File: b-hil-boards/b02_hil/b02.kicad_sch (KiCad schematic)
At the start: 13 parts, among them J2 Conn_01x06_Socket, K1 Relay_DPDT, K2 Relay_DPDT, K3 Relay_DPDT, K4 Relay_DPDT, U1 MAX485E, U2 ULN2003, U3 ADuM1412, U4 ESP32_C3_SuperMini, U5 OLED-128x64-I2C

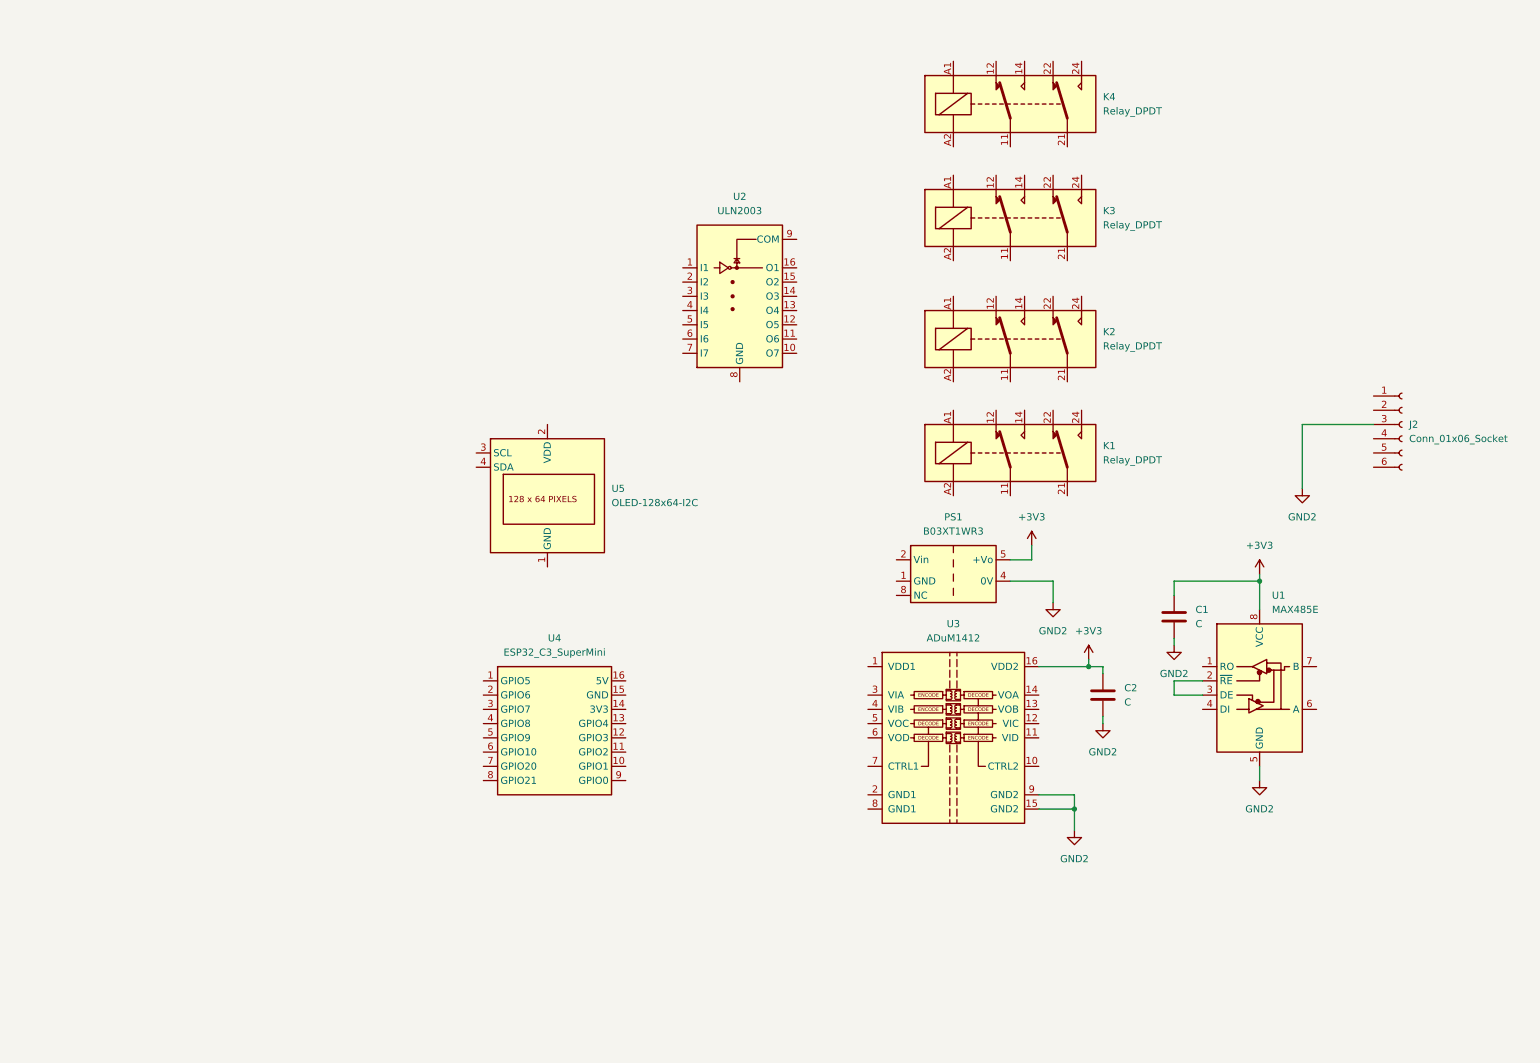
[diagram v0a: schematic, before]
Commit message: B02 card: routing and silkscreen completed
- PCB layout and silkscreen finished for b02_hil
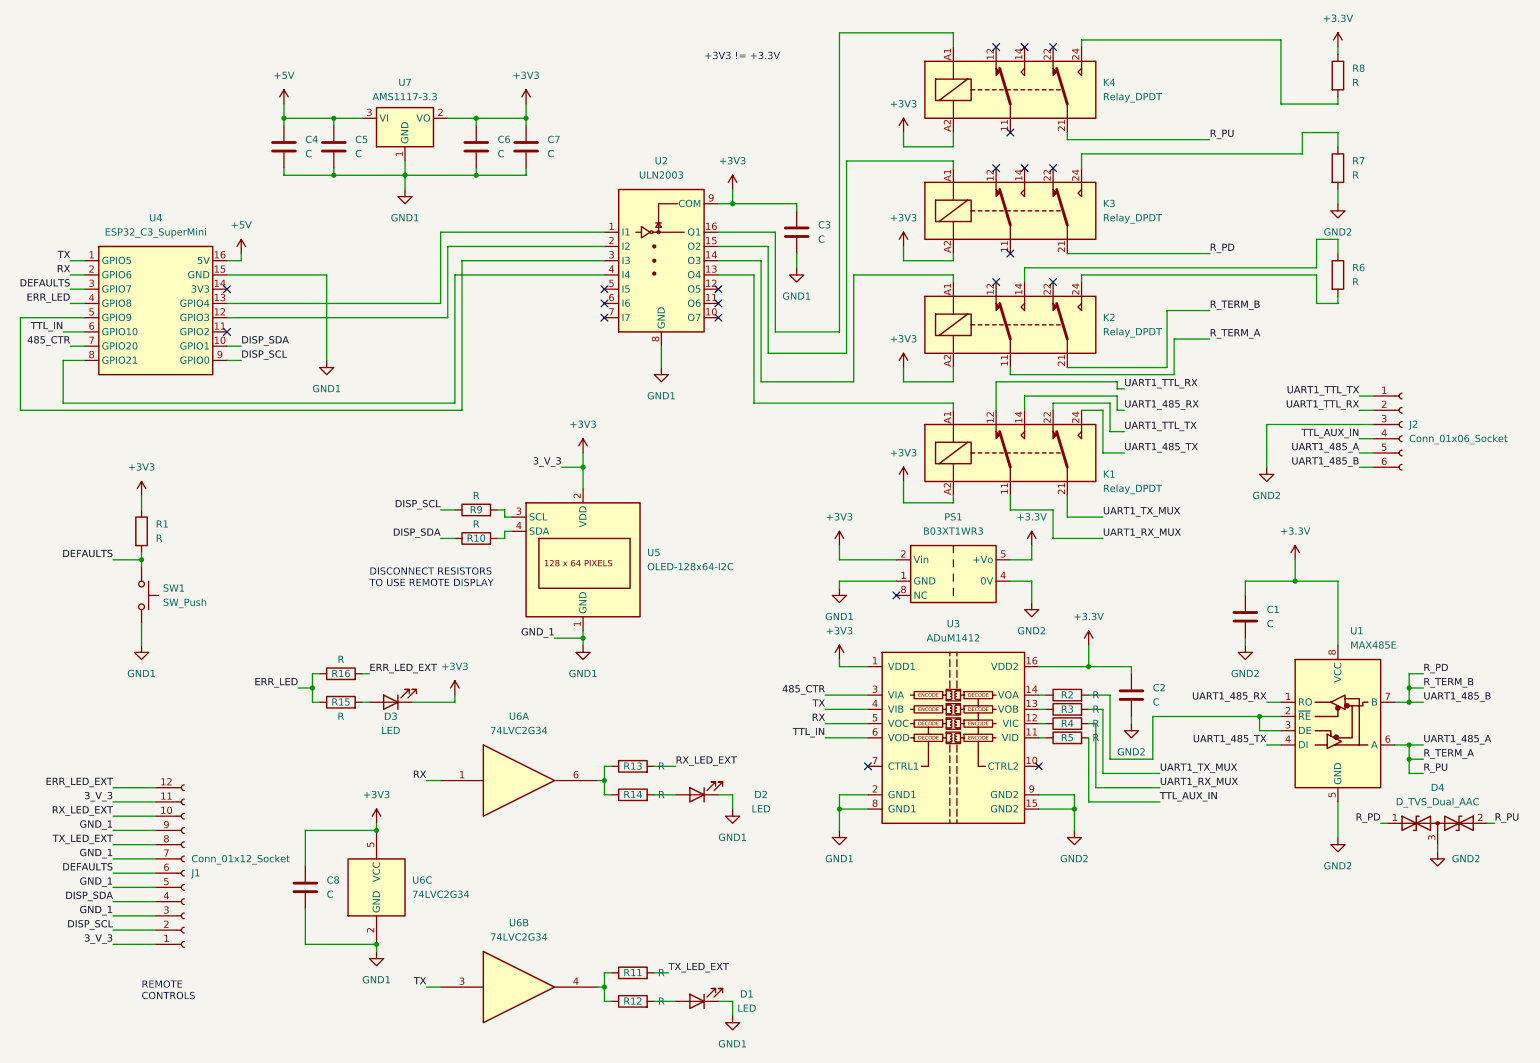
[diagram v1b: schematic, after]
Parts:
- added C3, C4, C5, C6, C7, C8: C, Capacitor_SMD:C_0805_2012Metric_Pad1.18x1.45mm_HandSolder, symbol Device:C
- added D1, D2, D3: LED, LED_SMD:LED_0805_2012Metric_Pad1.15x1.40mm_HandSolder, symbol Device:LED
- added D4: D_TVS_Dual_AAC, Package_TO_SOT_SMD:SOT-23-3, symbol Device:D_TVS_Dual_AAC
- added J1: Conn_01x12_Socket, TerminalBlock_DoubleLevel:TerminalBlock_DoubleLevel_2x06_P3.50mm_Horizontal, symbol Connector:Conn_01x12_Socket
- added R1, R10, R11, R12, R13, R14, R15, R16, R2, R3, R4, R5, R6, R7, R8, R9: R, Resistor_SMD:R_0805_2012Metric_Pad1.20x1.40mm_HandSolder, symbol Device:R
- added SW1: SW_Push, Button_Switch_SMD:SW_Push_1P1T_NO_6x6mm_H9.5mm, symbol Switch:SW_Push
- added U6: 74LVC2G34, Package_TO_SOT_SMD:SOT-23-6_Handsoldering, symbol 74xGxx:74LVC2G34
- added U7: AMS1117-3.3, Package_TO_SOT_SMD:SOT-223-3_TabPin2, symbol Regulator_Linear:AMS1117-3.3
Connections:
- net +3V3: now also K1.A2, K2.A2, K3.A2, K4.A2, PS1.2 (Vin), U2.9 (COM), U3.1 (VDD1), U5.2 (VDD), C3.1, C6.1, C7.1, C8.1, D3.1 (K), J1.1 (Pin_1), J1.11 (Pin_11), R1.1, U6.5 (VCC), U7.2 (VO); no longer C1.1, C2.1, PS1.5 (+Vo), U1.8 (VCC), U3.16 (VDD2)
- net GND2: now also D4.3 (common), R7.2
- net R_PU: now reaches K4.21
- net R_PU: now also J2.5 (Pin_5), K2.11, U1.6 (A), D4.2 (A2)
- net at K4.24: now also R8.2
- net at K4.A1: now also U2.16 (O1)
- net GND1: now reaches U5.1 (GND)
- net GND1: now also PS1.1 (GND), U2.8 (GND), U3.2 (GND1), U3.8 (GND1), U4.15 (GND), C3.2, C4.2, C5.2, C6.2, C7.2, C8.2, D1.1 (K), D2.1 (K), J1.3 (Pin_3), J1.5 (Pin_5), J1.7 (Pin_7), J1.9 (Pin_9), SW1.2, U6.2 (GND), U7.1 (GND)
- net at U5.3 (SCL): now also R9.2
- net at U5.4 (SDA): now also R10.2
- net UART1_TTL_TX: now reaches J2.1 (Pin_1)
- net UART1_TTL_TX: now also K1.22
- net UART1_TTL_RX: now reaches J2.2 (Pin_2)
- net UART1_TTL_RX: now also K1.12
- net TTL_AUX_IN: now reaches J2.4 (Pin_4)
- net TTL_AUX_IN: now also R5.2
- net R_PD: now reaches J2.6 (Pin_6)
- net R_PD: now also K2.21, K3.21, U1.7 (B), D4.1 (A1)
- net at U2.1 (I1): now also U4.13 (GPIO4)
- net at U2.13 (O4): now also K1.A1
- net at U2.14 (O3): now also K2.A1
- net at U2.15 (O2): now also K3.A1
- net at U2.2 (I2): now also U4.12 (GPIO3)
- net at U2.3 (I3): now also U4.5 (GPIO9)
- net at U2.4 (I4): now also U4.8 (GPIO21)
- net TX: now reaches U4.1 (GPIO5)
- net TX: now also U3.4 (VIB), U6.3
- net DISP_SDA: now reaches U4.10 (GPIO1)
- net DISP_SDA: now also J1.4 (Pin_4), R10.1
- net +5V: now reaches U4.16 (5V)
- net +5V: now also C4.1, C5.1, U7.3 (VI)
- net RX: now reaches U4.2 (GPIO6)
- net RX: now also U3.5 (VOC), U6.1
- net DEFAULTS: now reaches U4.3 (GPIO7)
- net DEFAULTS: now also J1.6 (Pin_6), R1.2, SW1.1
- net ERR_LED: now reaches U4.4 (GPIO8)
- net ERR_LED: now also R15.1, R16.1
- net TTL_IN: now reaches U4.6 (GPIO10)
- net TTL_IN: now also U3.6 (VOD)
- net 485_CTR: now reaches U4.7 (GPIO20)
- net 485_CTR: now also U3.3 (VIA)
- net DISP_SCL: now reaches U4.9 (GPIO0)
- net DISP_SCL: now also J1.2 (Pin_2), R9.1
- net at K2.14: now also R6.1
- net at K2.24: now also R6.2
- net at K3.24: now also R7.1
- net UART1_RX_MUX: now reaches K1.11
- net UART1_RX_MUX: now also R4.2
- net UART1_485_RX: now reaches K1.14
- net UART1_485_RX: now also U1.1 (RO)
- net UART1_TX_MUX: now reaches K1.21
- net UART1_TX_MUX: now also R3.2
- net UART1_485_TX: now reaches K1.24
- net UART1_485_TX: now also U1.4 (DI)
- net at U3.11 (VID): now also R5.1
- net at U3.12 (VIC): now also R4.1
- net at U3.13 (VOB): now also R3.1
- net at U3.14 (VOA): now also R2.1
- net at U1.2 (~{RE}), U1.3 (DE): now also R2.2
- new net: R13.1, R14.1, U6.6
- new net: D2.2 (A), R14.2
- new net: D1.2 (A), R12.2
- new net: R11.1, R12.1, U6.4
- new net: D3.2 (A), R15.2
- new net +3.3V: C1.1, C2.1, PS1.5 (+Vo), R8.1, U1.8 (VCC), U3.16 (VDD2)
- new net ERR_LED_EXT: J1.12 (Pin_12), R16.2
- new net RX_LED_EXT: J1.10 (Pin_10), R13.2
- new net TX_LED_EXT: J1.8 (Pin_8), R11.2
- no-connect marks 0 -> 21
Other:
- note added: "+3V3 != +3.3V"
- note added: "DISCONNECT RESISTORS TO USE REMOTE DISPLAY"
- note added: "REMOTE CONTROLS"
- moved on the sheet: C1, C2, K2, K3, K4, U1, U2, U4, U5

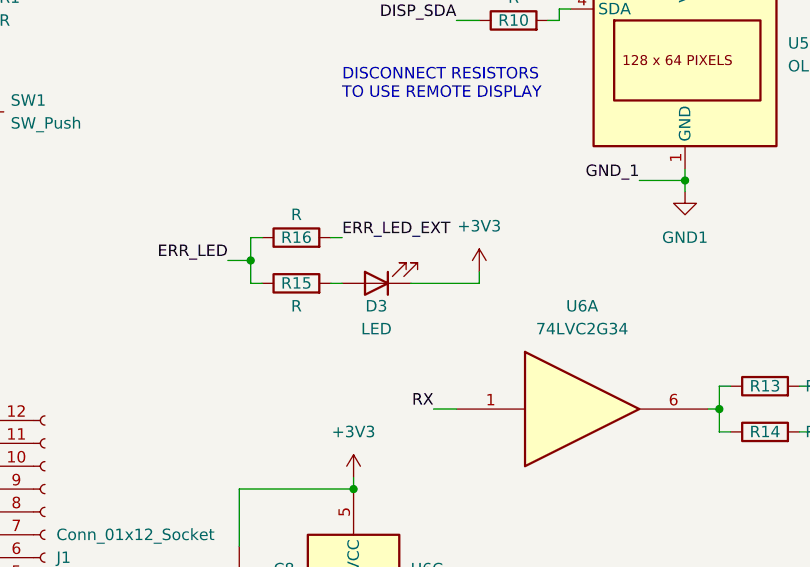
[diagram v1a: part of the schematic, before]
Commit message: fix(b02): correct LED D3 polarity on schematic and PCB
Fix reversed polarity marking/connection for D3 in b02.kicad_sch and
b02.kicad_pcb.
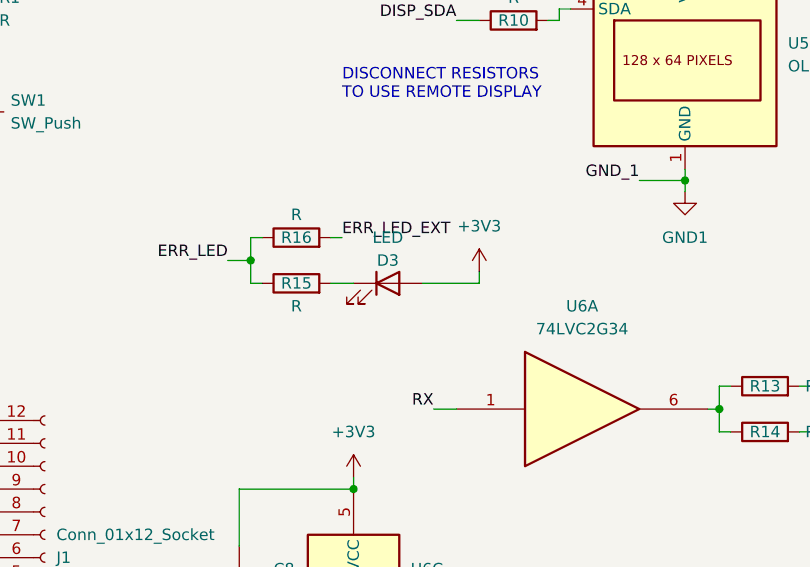
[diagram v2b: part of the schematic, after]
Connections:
- net +3V3: now also D3.2 (A); no longer D3.1 (K)
- net at R15.2: now also D3.1 (K); no longer D3.2 (A)
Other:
- moved on the sheet: D3
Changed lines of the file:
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@@
+    (stroke (width 0) (type default))
+  )
+  (wire (pts (xy 86.36 135.89) (xy 92.71 135.89))
     (stroke (width 0) (type default))
   )
@@
     (stroke (width 0) (type default))
   )
-  (wire (pts (xy 76.2 135.89) (xy 77.47 135.89))
-    (stroke (width 0) (type default))
-  )
   (wire (pts (xy 31.75 176.53) (xy 39.37 176.53))
     (stroke (width 0) (type default))
@@
     (stroke (width 0) (type default))
   )
+  (wire (pts (xy 76.2 135.89) (xy 78.74 135.89))
+    (stroke (width 0) (type default))
+  )
   (wire (pts (xy 237.49 86.36) (xy 256.54 86.36))
     (stroke (width 0) (type default))
@@
   )
   (wire (pts (xy 196.85 152.4) (xy 203.2 152.4))
-    (stroke (width 0) (type default))
-  )
-  (wire (pts (xy 85.09 135.89) (xy 92.71 135.89))
     (stroke (width 0) (type default))
   )
@@
     )
   )
-  (symbol (lib_id "Device:LED") (at 81.28 135.89 180) (unit 1)
+  (symbol (lib_id "Device:LED") (at 82.55 135.89 0) (unit 1)
     (in_bom yes) (on_board yes) (dnp no)
-    (property "Reference" "D3" (at 81.28 138.43 0)
-      (effects (font (size 1.27 1.27)))
-    )
-    (property "Value" "LED" (at 81.28 140.97 0)
-      (effects (font (size 1.27 1.27)))
-    )
-    (property "Footprint" "LED_SMD:LED_0805_2012Metric_Pad1.15x1.40mm_HandSolder" (at 81.28 135.89 0)
-      (effects (font (size 1.27 1.27)) hide)
-    )
-    (property "Datasheet" "~" (at 81.28 135.89 0)
-      (effects (font (size 1.27 1.27)) hide)
-    )
+    (property "Reference" "D3" (at 82.55 133.35 0)
+      (effects (font (size 1.27 1.27)))
+    )
+    (property "Value" "LED" (at 82.55 130.81 0)
+      (effects (font (size 1.27 1.27)))
+    )
+    (property "Footprint" "LED_SMD:LED_0805_2012Metric_Pad1.15x1.40mm_HandSolder" (at 82.55 135.89 0)
+      (effects (font (size 1.27 1.27)) hide)
+    )
+    (property "Datasheet" "~" (at 82.55 135.89 0)
+      (effects (font (size 1.27 1.27)) hide)
+    )

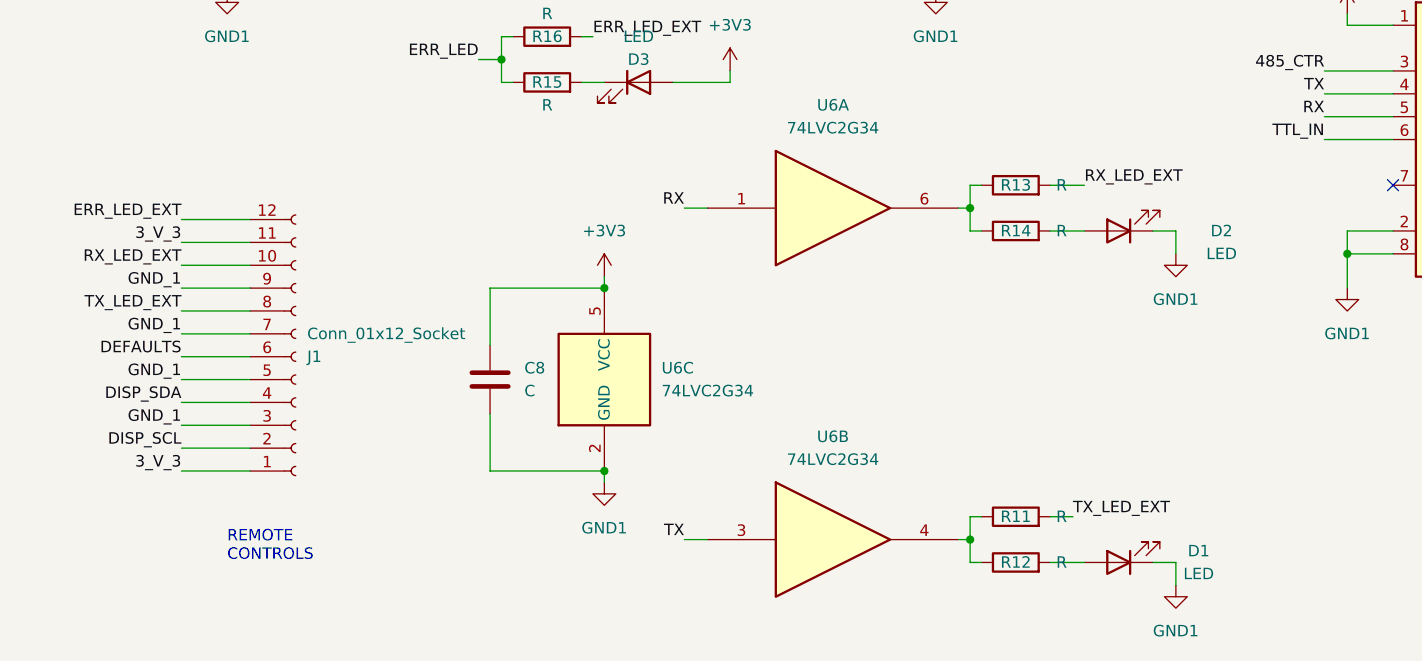
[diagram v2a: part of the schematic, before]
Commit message: B02: invert UART indicator LED polarity; refresh KiCad backups
- B02: reflect UART status LED polarity in schematic and PCB; update project layout.
- B02/B03/B04: rotate KiCad automatic backup zips (remove obsolete B02 backups, add current ones).
- B03: tweak D7 silkscreen/Fab text offsets on PCB (reference and value placement).
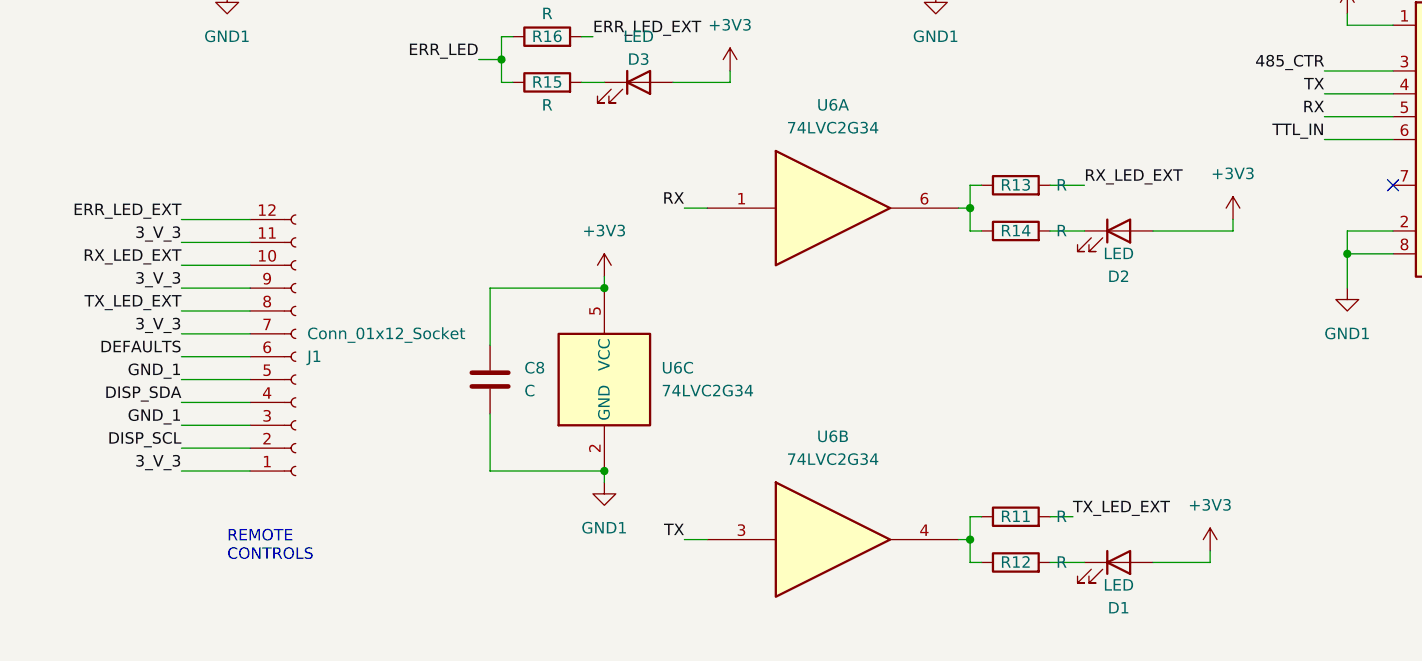
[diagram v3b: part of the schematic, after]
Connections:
- net +3V3: now also D1.2 (A), D2.2 (A), J1.7 (Pin_7), J1.9 (Pin_9)
- net GND1: no longer D1.1 (K), D2.1 (K), J1.7 (Pin_7), J1.9 (Pin_9)
- net at R14.2: now also D2.1 (K); no longer D2.2 (A)
- net at R12.2: now also D1.1 (K); no longer D1.2 (A)
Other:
- moved on the sheet: D1, D2
